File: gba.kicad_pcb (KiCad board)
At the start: 2 copper layers, 41 parts, among them IC10 nRF52832-QFAA-R7, IC2 MT41K256M16TW-107_P, IC3 STC3117IJT, IC4 MCP73830T-2AAI_MYY, IC5 MT41K256M16TW-107_P, IC6 STPMIC1BPQR, IC8 STUSB1600AQTR, Q1 PMDPB70XP_115

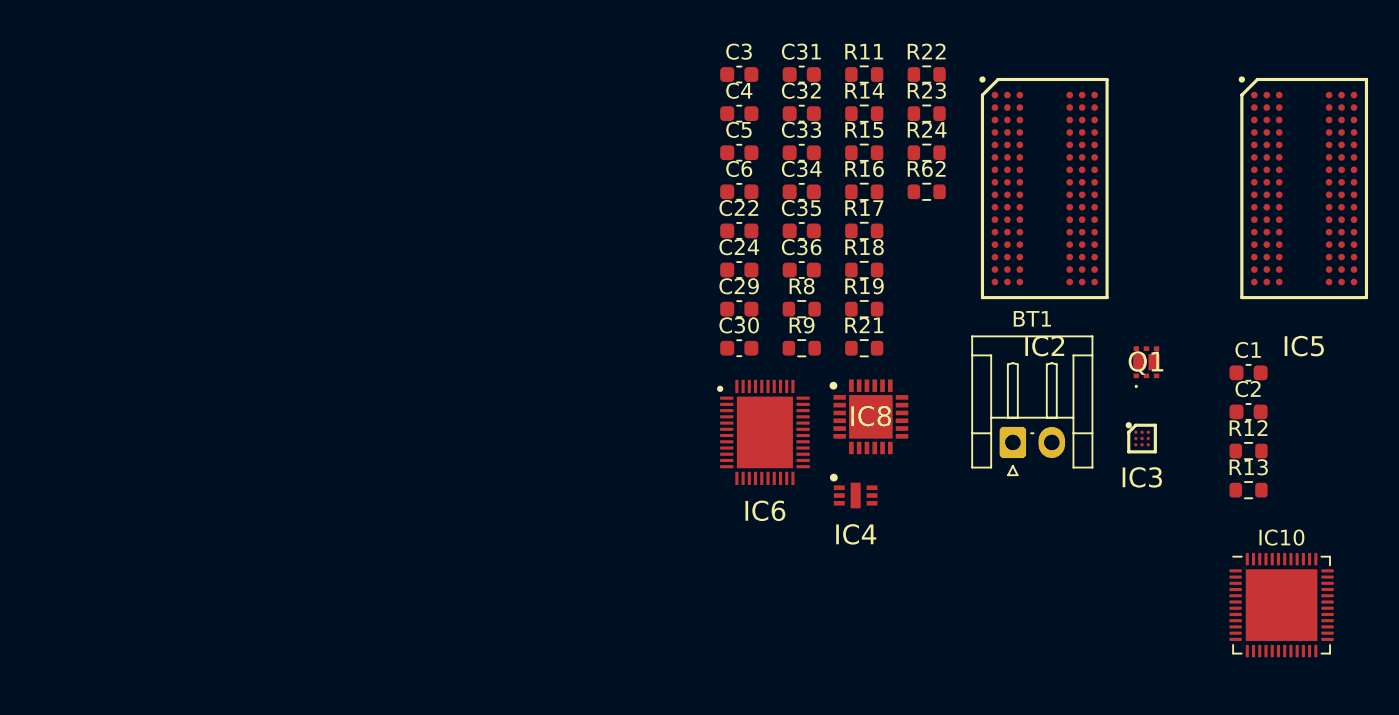
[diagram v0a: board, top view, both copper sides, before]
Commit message: Added UART to 1YN
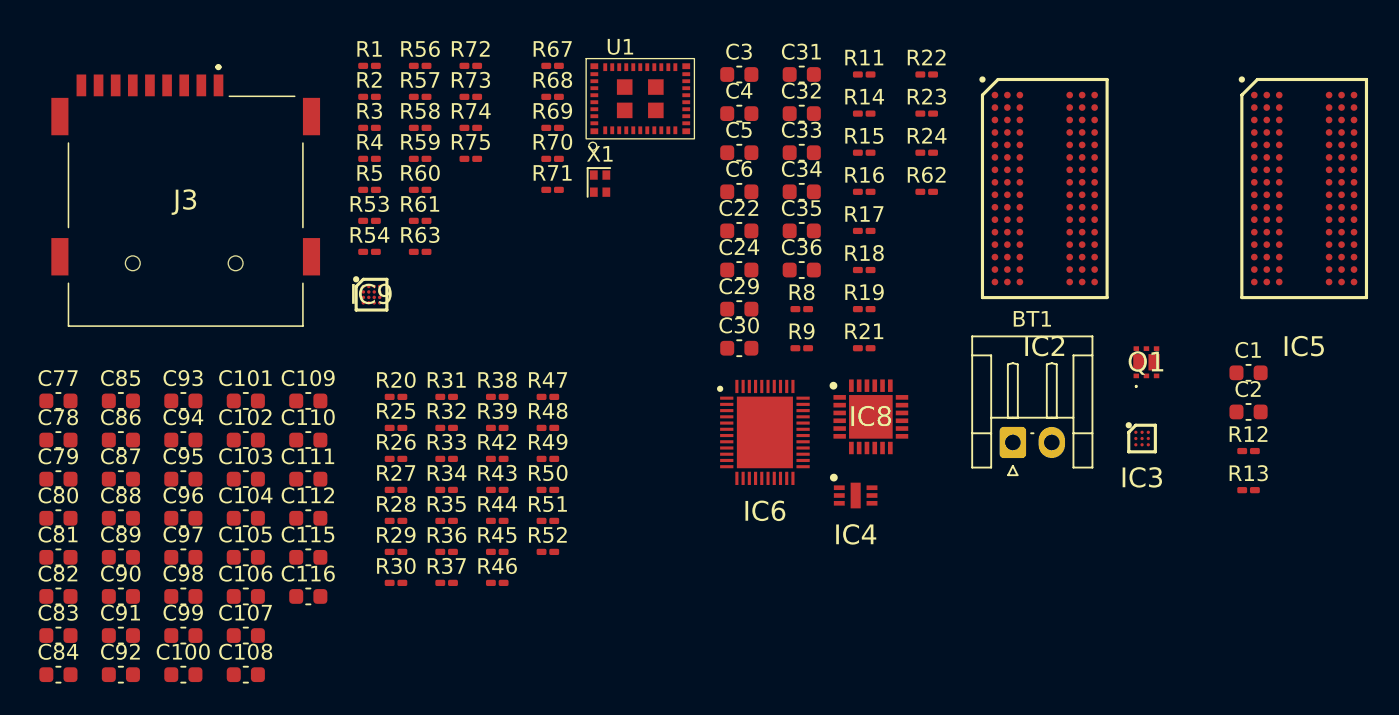
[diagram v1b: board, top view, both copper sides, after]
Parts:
- removed IC10: nRF52832-QFAA-R7, Package_DFN_QFN:QFN-48-1EP_6x6mm_P0.4mm_EP4.6x4.6mm
- added C100: 1u, Capacitor_SMD:C_0603_1608Metric, F.Cu at (43.9, 92.2)
- added C101: 1u, Capacitor_SMD:C_0603_1608Metric, F.Cu at (47.9, 74.6)
- added C102: 1u, Capacitor_SMD:C_0603_1608Metric, F.Cu at (47.9, 77.1)
- added C103: 1u, Capacitor_SMD:C_0603_1608Metric, F.Cu at (47.9, 79.6)
- added C104: 1u, Capacitor_SMD:C_0603_1608Metric, F.Cu at (47.9, 82.1)
- added C105: 1u, Capacitor_SMD:C_0603_1608Metric, F.Cu at (47.9, 84.7)
- added C106: 2u2, Capacitor_SMD:C_0603_1608Metric, F.Cu at (47.9, 87.2)
- added C107: 2u2, Capacitor_SMD:C_0603_1608Metric, F.Cu at (47.9, 89.7)
- added C108: 1u, Capacitor_SMD:C_0603_1608Metric, F.Cu at (47.9, 92.2)
- added C109: 2u2, Capacitor_SMD:C_0603_1608Metric, F.Cu at (51.9, 74.6)
- added C110: 1u, Capacitor_SMD:C_0603_1608Metric, F.Cu at (51.9, 77.1)
- added C111: 1u, Capacitor_SMD:C_0603_1608Metric, F.Cu at (51.9, 79.6)
- added C112: 100n, Capacitor_SMD:C_0603_1608Metric, F.Cu at (51.9, 82.1)
- added C115: 1u, Capacitor_SMD:C_0603_1608Metric, F.Cu at (51.9, 84.7)
- added C116: 100n, Capacitor_SMD:C_0603_1608Metric, F.Cu at (51.9, 87.2)
- added C77: 100n, Capacitor_SMD:C_0603_1608Metric, F.Cu at (35.9, 74.6)
- added C78: 1u, Capacitor_SMD:C_0603_1608Metric, F.Cu at (35.9, 77.1)
- added C79: 1u, Capacitor_SMD:C_0603_1608Metric, F.Cu at (35.9, 79.6)
- added C80: 1u, Capacitor_SMD:C_0603_1608Metric, F.Cu at (35.9, 82.1)
- added C81: 1u, Capacitor_SMD:C_0603_1608Metric, F.Cu at (35.9, 84.7)
- added C82: 1u, Capacitor_SMD:C_0603_1608Metric, F.Cu at (35.9, 87.2)
- added C83: 1u, Capacitor_SMD:C_0603_1608Metric, F.Cu at (35.9, 89.7)
- added C84: 1u, Capacitor_SMD:C_0603_1608Metric, F.Cu at (35.9, 92.2)
- added C85: 1u, Capacitor_SMD:C_0603_1608Metric, F.Cu at (39.9, 74.6)
- added C86: 1u, Capacitor_SMD:C_0603_1608Metric, F.Cu at (39.9, 77.1)
- added C87: 1u, Capacitor_SMD:C_0603_1608Metric, F.Cu at (39.9, 79.6)
- added C88: 1u, Capacitor_SMD:C_0603_1608Metric, F.Cu at (39.9, 82.1)
- added C89: 1u, Capacitor_SMD:C_0603_1608Metric, F.Cu at (39.9, 84.7)
- added C90: 1u, Capacitor_SMD:C_0603_1608Metric, F.Cu at (39.9, 87.2)
- added C91: 1u, Capacitor_SMD:C_0603_1608Metric, F.Cu at (39.9, 89.7)
- added C92: 1u, Capacitor_SMD:C_0603_1608Metric, F.Cu at (39.9, 92.2)
- added C93: 1u, Capacitor_SMD:C_0603_1608Metric, F.Cu at (43.9, 74.6)
- added C94: 1u, Capacitor_SMD:C_0603_1608Metric, F.Cu at (43.9, 77.1)
- added C95: 1u, Capacitor_SMD:C_0603_1608Metric, F.Cu at (43.9, 79.6)
- added C96: 1u, Capacitor_SMD:C_0603_1608Metric, F.Cu at (43.9, 82.1)
- added C97: 1n, Capacitor_SMD:C_0603_1608Metric, F.Cu at (43.9, 84.7)
- added C98: 1n, Capacitor_SMD:C_0603_1608Metric, F.Cu at (43.9, 87.2)
- added C99: 1u, Capacitor_SMD:C_0603_1608Metric, F.Cu at (43.9, 89.7)
- added IC9: NXS0506UPZ, FuckOff:BGA16C35P4X4_146X146X47, F.Cu at (56.0, 67.8)
- added J3: MEM2075-00-140-01-A, FuckOff:MEM20750014001A, F.Cu at (44.1, 62.1)
- added R1: 0R, Resistor_SMD:R_0201_0603Metric_Pad0.64x0.40mm_HandSolder, F.Cu at (55.9, 53.1)
- added R2: 1k, Resistor_SMD:R_0201_0603Metric_Pad0.64x0.40mm_HandSolder, F.Cu at (55.9, 55.1)
- added R20: 240R, Resistor_SMD:R_0201_0603Metric_Pad0.64x0.40mm_HandSolder, F.Cu at (57.6, 74.3)
- added R25: 56R, Resistor_SMD:R_0201_0603Metric_Pad0.64x0.40mm_HandSolder, F.Cu at (57.6, 76.3)
- added R26: 56R, Resistor_SMD:R_0201_0603Metric_Pad0.64x0.40mm_HandSolder, F.Cu at (57.6, 78.3)
- added R27: 56R, Resistor_SMD:R_0201_0603Metric_Pad0.64x0.40mm_HandSolder, F.Cu at (57.6, 80.3)
- added R28: 56R, Resistor_SMD:R_0201_0603Metric_Pad0.64x0.40mm_HandSolder, F.Cu at (57.6, 82.3)
- added R29: 56R, Resistor_SMD:R_0201_0603Metric_Pad0.64x0.40mm_HandSolder, F.Cu at (57.6, 84.3)
- added R3: 0R, Resistor_SMD:R_0201_0603Metric_Pad0.64x0.40mm_HandSolder, F.Cu at (55.9, 57.1)
- added R30: 56R, Resistor_SMD:R_0201_0603Metric_Pad0.64x0.40mm_HandSolder, F.Cu at (57.6, 86.3)
- added R31: 56R, Resistor_SMD:R_0201_0603Metric_Pad0.64x0.40mm_HandSolder, F.Cu at (60.8, 74.3)
- added R32: 56R, Resistor_SMD:R_0201_0603Metric_Pad0.64x0.40mm_HandSolder, F.Cu at (60.8, 76.3)
- added R33: 56R, Resistor_SMD:R_0201_0603Metric_Pad0.64x0.40mm_HandSolder, F.Cu at (60.8, 78.3)
- added R34: 56R, Resistor_SMD:R_0201_0603Metric_Pad0.64x0.40mm_HandSolder, F.Cu at (60.8, 80.3)
- added R35: 56R, Resistor_SMD:R_0201_0603Metric_Pad0.64x0.40mm_HandSolder, F.Cu at (60.8, 82.3)
- added R36: 56R, Resistor_SMD:R_0201_0603Metric_Pad0.64x0.40mm_HandSolder, F.Cu at (60.8, 84.3)
- added R37: 56R, Resistor_SMD:R_0201_0603Metric_Pad0.64x0.40mm_HandSolder, F.Cu at (60.8, 86.3)
- added R38: 56R, Resistor_SMD:R_0201_0603Metric_Pad0.64x0.40mm_HandSolder, F.Cu at (64.1, 74.3)
- added R39: 56R, Resistor_SMD:R_0201_0603Metric_Pad0.64x0.40mm_HandSolder, F.Cu at (64.1, 76.3)
- added R4: 1k, Resistor_SMD:R_0201_0603Metric_Pad0.64x0.40mm_HandSolder, F.Cu at (55.9, 59.1)
- added R42: 100R, Resistor_SMD:R_0201_0603Metric_Pad0.64x0.40mm_HandSolder, F.Cu at (64.1, 78.3)
- added R43: 56R, Resistor_SMD:R_0201_0603Metric_Pad0.64x0.40mm_HandSolder, F.Cu at (64.1, 80.3)
- added R44: 56R, Resistor_SMD:R_0201_0603Metric_Pad0.64x0.40mm_HandSolder, F.Cu at (64.1, 82.3)
- added R45: 56R, Resistor_SMD:R_0201_0603Metric_Pad0.64x0.40mm_HandSolder, F.Cu at (64.1, 84.3)
- added R46: 56R, Resistor_SMD:R_0201_0603Metric_Pad0.64x0.40mm_HandSolder, F.Cu at (64.1, 86.3)
- added R47: 56R, Resistor_SMD:R_0201_0603Metric_Pad0.64x0.40mm_HandSolder, F.Cu at (67.3, 74.3)
- added R48: 56R, Resistor_SMD:R_0201_0603Metric_Pad0.64x0.40mm_HandSolder, F.Cu at (67.3, 76.3)
- added R49: 56R, Resistor_SMD:R_0201_0603Metric_Pad0.64x0.40mm_HandSolder, F.Cu at (67.3, 78.3)
- added R5: 0R, Resistor_SMD:R_0201_0603Metric_Pad0.64x0.40mm_HandSolder, F.Cu at (55.9, 61.1)
- added R50: 56R, Resistor_SMD:R_0201_0603Metric_Pad0.64x0.40mm_HandSolder, F.Cu at (67.3, 80.3)
- added R51: 56R, Resistor_SMD:R_0201_0603Metric_Pad0.64x0.40mm_HandSolder, F.Cu at (67.3, 82.3)
- added R52: 240R, Resistor_SMD:R_0201_0603Metric_Pad0.64x0.40mm_HandSolder, F.Cu at (67.3, 84.3)
- added R53: 0R, Resistor_SMD:R_0201_0603Metric_Pad0.64x0.40mm_HandSolder, F.Cu at (55.9, 63.0)
- added R54: 0R, Resistor_SMD:R_0201_0603Metric_Pad0.64x0.40mm_HandSolder, F.Cu at (55.9, 65.0)
- added R56: 47k, Resistor_SMD:R_0201_0603Metric_Pad0.64x0.40mm_HandSolder, F.Cu at (59.1, 53.1)
- added R57: 47k, Resistor_SMD:R_0201_0603Metric_Pad0.64x0.40mm_HandSolder, F.Cu at (59.1, 55.1)
- added R58: 47k, Resistor_SMD:R_0201_0603Metric_Pad0.64x0.40mm_HandSolder, F.Cu at (59.1, 57.1)
- added R59: 47k, Resistor_SMD:R_0201_0603Metric_Pad0.64x0.40mm_HandSolder, F.Cu at (59.1, 59.1)
- added R60: 47k, Resistor_SMD:R_0201_0603Metric_Pad0.64x0.40mm_HandSolder, F.Cu at (59.1, 61.1)
- added R61: 47k, Resistor_SMD:R_0201_0603Metric_Pad0.64x0.40mm_HandSolder, F.Cu at (59.1, 63.0)
- added R63: 1k, Resistor_SMD:R_0201_0603Metric_Pad0.64x0.40mm_HandSolder, F.Cu at (59.1, 65.0)
- added R67: 10K, Resistor_SMD:R_0201_0603Metric_Pad0.64x0.40mm_HandSolder, F.Cu at (67.6, 53.1)
- added R68: 10K, Resistor_SMD:R_0201_0603Metric_Pad0.64x0.40mm_HandSolder, F.Cu at (67.6, 55.1)
- added R69: 10K, Resistor_SMD:R_0201_0603Metric_Pad0.64x0.40mm_HandSolder, F.Cu at (67.6, 57.1)
- added R70: 10K, Resistor_SMD:R_0201_0603Metric_Pad0.64x0.40mm_HandSolder, F.Cu at (67.6, 59.1)
- added R71: 10K, Resistor_SMD:R_0201_0603Metric_Pad0.64x0.40mm_HandSolder, F.Cu at (67.6, 61.1)
- added R72: 0R, Resistor_SMD:R_0201_0603Metric_Pad0.64x0.40mm_HandSolder, F.Cu at (62.4, 53.1)
- added R73: 0R, Resistor_SMD:R_0201_0603Metric_Pad0.64x0.40mm_HandSolder, F.Cu at (62.4, 55.1)
- added R74: 0R, Resistor_SMD:R_0201_0603Metric_Pad0.64x0.40mm_HandSolder, F.Cu at (62.4, 57.1)
- added R75: 0R, Resistor_SMD:R_0201_0603Metric_Pad0.64x0.40mm_HandSolder, F.Cu at (62.4, 59.1)
- added U1: ~, ARMband:Murata 1YN, F.Cu at (73.2, 55.2)
- added X1: ASCO, Oscillator:Oscillator_SMD_Abracon_ASCO-4Pin_1.6x1.2mm, F.Cu at (70.7, 60.7)
- R11, R12, R13, R14, R15, R16, R17, R18, R19, R21, R22, R23, R24, R62, R8, R9: footprint Resistor_SMD:R_0603_1608Metric -> Resistor_SMD:R_0201_0603Metric_Pad0.64x0.40mm_HandSolder
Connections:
- net GND renamed GND_SR_PVSS
- IC6 pad 1: unconnected-(IC6-RSTN-Pad1) -> Net-(IC6-RSTN)
- IC6 pad 17: unconnected-(IC6-PONKEYN-Pad17) -> Net-(IC6-PONKEYN)
- IC6 pad 2: unconnected-(IC6-WAKEUP-Pad2) -> PMIC_WAKEUP
- IC6 pad 3: Net-(IC6-SDA) -> SDA
- IC6 pad 39: VDD_USB -> MP1_VDD_USB
- IC6 pad 4: Net-(IC6-SCL) -> SCL
- IC6 pad 43: unconnected-(IC6-INTN-Pad43) -> PMIC_INT
- IC6 pad 44: unconnected-(IC6-PWRCTRL-Pad44) -> Net-(IC6-PWRCTRL)
